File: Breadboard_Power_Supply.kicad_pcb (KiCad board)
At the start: 2 copper layers, 30 x 60 mm, 22 parts, among them J1 9V Battery, J2 USB_B, J3 Barrel_Jack_Switch, J4 1, J5 2, J6 3, SW1 SW_DIP_x03, U1 AMS1117-5.0, U2 AMS1117-3.3

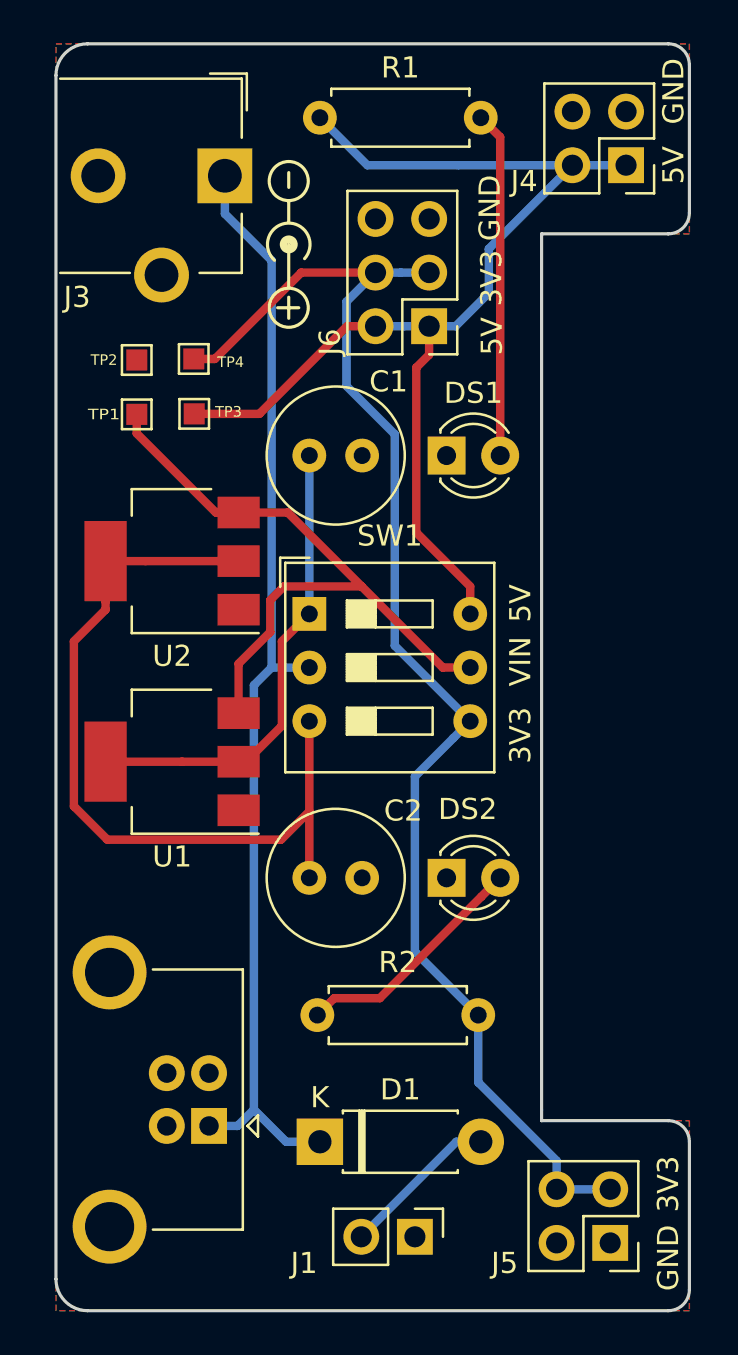
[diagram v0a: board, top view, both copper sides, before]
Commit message: Markings improved
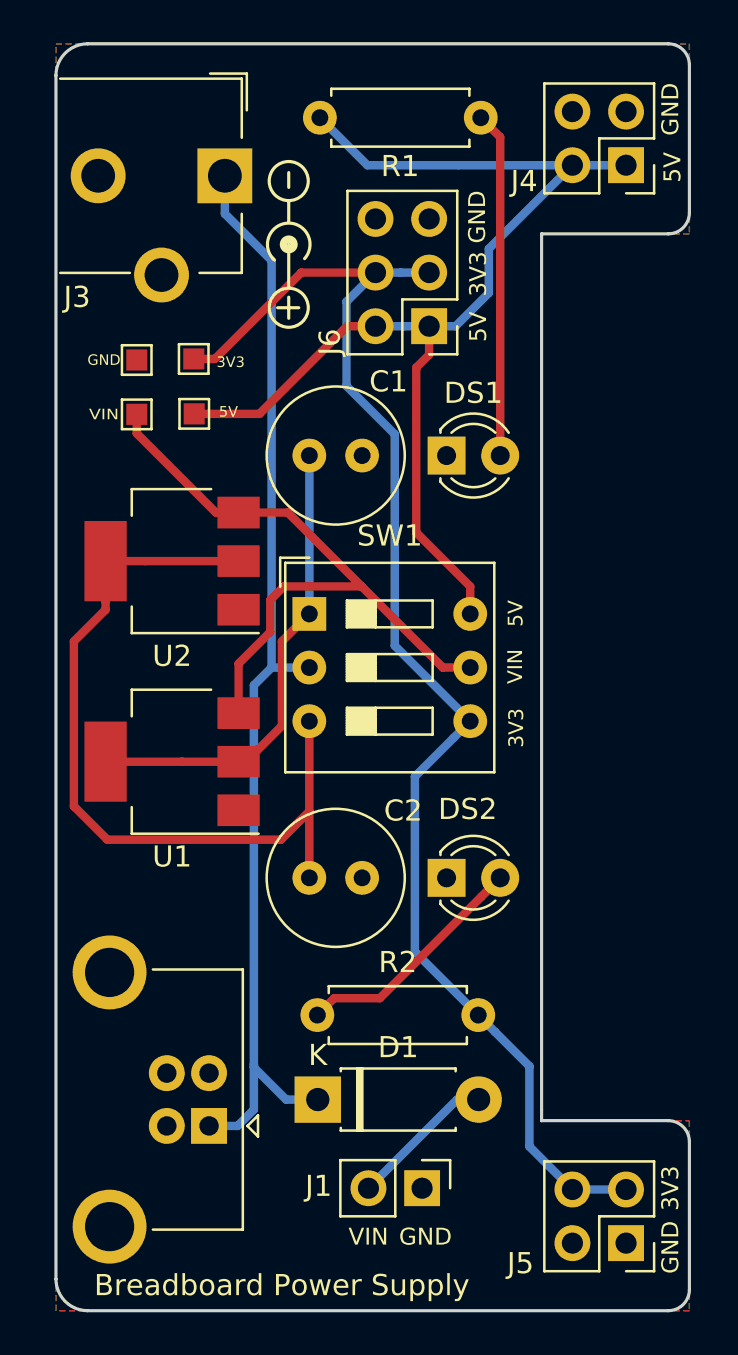
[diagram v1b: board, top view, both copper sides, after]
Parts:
- removed OSH: OSHW-Logo2_7.3x6mm_SilkScreen, Symbol:OSHW-Logo2_7.3x6mm_SilkScreen
- added REF**: OSHW-Logo2_7.3x6mm_SilkScreen, Symbol:OSHW-Logo2_7.3x6mm_SilkScreen, B.Cu at (148.9, 63.3)
-  5V: renamed from TP3
- moved J1 2.32 mm to (149.8, 113.7)
- moved D1 2.00 mm to (144.9, 109.5)
- moved J5 0.75 mm to (159.5, 116.3)
- renumbered TP4 to 3V3, TP2 to GND, TP1 to VIN
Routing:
- net Net-(D1-Pad2): track 7.52 -> 6.96 mm
